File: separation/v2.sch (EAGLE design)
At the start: 0 parts

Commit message: add mcu
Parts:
- added JP2, JP4: (no value), microbuilder:HEADER-1X7
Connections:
- new net +3V3: JP4.5
- new net A0: JP2.1
- new net A1: JP2.2
- new net A2: JP2.3
- new net A3: JP2.4
- new net GND: JP4.6
- new net MISO: JP4.3
- new net MOSI: JP4.4
- new net RX: JP4.1
- new net SCK: JP4.2
- new net SCL: JP2.6
- new net SDA: JP2.5
- new net TX: JP2.7
- new net VCC: JP4.7
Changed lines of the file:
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@@
 </classes>
 <parts>
+<part name="JP2" library="microbuilder" deviceset="HEADER-1X7" device=""/>
+<part name="GND1" library="supply1" library_urn="urn:adsk.eagle:library:371" deviceset="GND" device=""/>
+<part name="JP4" library="microbuilder" deviceset="HEADER-1X7" device=""/>
+<part name="+3V1" library="supply1" library_urn="urn:adsk.eagle:library:371" deviceset="+3V3" device=""/>
 </parts>
 <sheets>
@@
 </plain>
 <instances>
+<instance part="JP2" gate="A" x="60.96" y="58.42" smashed="yes">
+<attribute name="NAME" x="54.61" y="69.215" size="1.778" layer="95"/>
+<attribute name="VALUE" x="54.61" y="45.72" size="1.778" layer="96"/>
+</instance>
+<instance part="GND1" gate="1" x="10.16" y="60.96" smashed="yes" rot="MR0">
+<attribute name="VALUE" x="12.7" y="58.42" size="1.778" layer="96" rot="MR0"/>
+</instance>
+<instance part="JP4" gate="A" x="38.1" y="58.42" smashed="yes" rot="MR180">
+<attribute name="NAME" x="31.75" y="47.625" size="1.778" layer="95" rot="MR180"/>
+<attribute name="VALUE" x="31.75" y="71.12" size="1.778" layer="96" rot="MR180"/>
+</instance>
+<instance part="+3V1" gate="G$1" x="15.24" y="60.96" smashed="yes" rot="R90">
+<attribute name="VALUE" x="20.32" y="58.42" size="1.778" layer="96" rot="R180"/>
+</instance>
 </instances>
 <busses>
 </busses>
 <nets>
+<net name="GND" class="1">
+<segment>
+<wire x1="35.56" y1="63.5" x2="10.16" y2="63.5" width="0.1524" layer="91"/>
+<pinref part="GND1" gate="1" pin="GND"/>
+<pinref part="JP4" gate="A" pin="6"/>
+</segment>
+</net>
+<net name="MOSI" class="0">
+<segment>
+<wire x1="35.56" y1="58.42" x2="17.78" y2="58.42" width="0.1524" layer="91"/>
+<label x="20.32" y="58.42" size="1.778" layer="95"/>
+<pinref part="JP4" gate="A" pin="4"/>
+</segment>
+</net>
+<net name="MISO" class="0">
+<segment>
+<wire x1="35.56" y1="55.88" x2="17.78" y2="55.88" width="0.1524" layer="91"/>
+<label x="20.32" y="55.88" size="1.778" layer="95"/>
+<pinref part="JP4" gate="A" pin="3"/>
+</segment>
+</net>
+<net name="SCK" class="0">
+<segment>
+<wire x1="35.56" y1="53.34" x2="17.78" y2="53.34" width="0.1524" layer="91"/>
+<label x="20.32" y="53.34" size="1.778" layer="95"/>
+<pinref part="JP4" gate="A" pin="2"/>
+</segment>
+</net>
+<net name="A3" class="0">
+<segment>
+<label x="45.72" y="58.42" size="1.778" layer="95"/>
+<pinref part="JP2" gate="A" pin="4"/>
+<wire x1="58.42" y1="58.42" x2="45.72" y2="58.42" width="0.1524" layer="91"/>
+</segment>
+</net>
+<net name="A2" class="0">
+<segment>
+<label x="45.72" y="60.96" size="1.778" layer="95"/>
+<pinref part="JP2" gate="A" pin="3"/>
+<wire x1="45.72" y1="60.96" x2="58.42" y2="60.96" width="0.1524" layer="91"/>
+</segment>
+</net>
+<net name="A1" class="0">
+<segment>
+<pinref part="JP2" gate="A" pin="2"/>
+<wire x1="58.42" y1="63.5" x2="45.72" y2="63.5" width="0.1524" layer="91"/>
+<label x="45.72" y="63.5" size="1.778" layer="95"/>
+</segment>
+</net>
+<net name="+3V3" class="0">
+<segment>
+<wire x1="35.56" y1="60.96" x2="17.78" y2="60.96" width="0.1524" layer="91"/>
+<pinref part="JP4" gate="A" pin="5"/>
+<pinref part="+3V1" gate="G$1" pin="+3V3"/>
+</segment>
+</net>
+<net name="A0" class="0">
+<segment>
+<label x="45.72" y="66.04" size="1.778" layer="95"/>
+<pinref part="JP2" gate="A" pin="1"/>
+<wire x1="45.72" y1="66.04" x2="58.42" y2="66.04" width="0.1524" layer="91"/>
+</segment>
+</net>
+<net name="SCL" class="0">
+<segment>
+<pinref part="JP2" gate="A" pin="6"/>
+<wire x1="58.42" y1="53.34" x2="45.72" y2="53.34" width="0.1524" layer="91"/>
+<label x="45.72" y="53.34" size="1.778" layer="95"/>
+</segment>
+</net>
+<net name="SDA" class="0">
+<segment>
+<pinref part="JP2" gate="A" pin="5"/>
+<wire x1="45.72" y1="55.88" x2="58.42" y2="55.88" width="0.1524" layer="91"/>
+<label x="45.72" y="55.88" size="1.778" layer="95"/>
+</segment>
+</net>
+<net name="TX" class="0">
+<segment>
+<pinref part="JP2" gate="A" pin="7"/>
+<wire x1="58.42" y1="50.8" x2="45.72" y2="50.8" width="0.1524" layer="91"/>
+<label x="45.72" y="50.8" size="1.778" layer="95"/>
+</segment>
+</net>
+<net name="RX" class="0">
+<segment>
+<wire x1="35.56" y1="50.8" x2="17.78" y2="50.8" width="0.1524" layer="91"/>
+<label x="20.32" y="50.8" size="1.778" layer="95"/>
+<pinref part="JP4" gate="A" pin="1"/>
+</segment>
+</net>
+<net name="VCC" class="1">
+<segment>
+<wire x1="35.56" y1="66.04" x2="17.78" y2="66.04" width="0.1524" layer="91"/>
+<wire x1="17.78" y1="66.04" x2="17.78" y2="73.66" width="0.1524" layer="91"/>
+<pinref part="JP4" gate="A" pin="7"/>
+<label x="22.86" y="73.66" size="1.778" layer="95"/>
+</segment>
+</net>
 </nets>
 </sheet>
@@
 </schematic>
 </drawing>
+<compatibility>
+<note version="8.2" severity="warning">
+Since Version 8.2, EAGLE supports online libraries. The ids
+of those online libraries will not be understood (or retained)
+with this version.
+</note>
+<note version="8.3" severity="warning">
+Since Version 8.3, EAGLE supports URNs for individual library
+assets (packages, symbols, and devices). The URNs of those assets
+will not be understood (or retained) with this version.
+</note>
+</compatibility>
 </eagle>

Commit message: 9mm buzzer
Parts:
- added LS1: KSTG931AP, SamacSys_Parts:KSTG931AP
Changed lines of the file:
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@@
 <part name="JP4" library="microbuilder" deviceset="HEADER-1X7" device=""/>
 <part name="+3V1" library="supply1" library_urn="urn:adsk.eagle:library:371" deviceset="+3V3" device=""/>
+<part name="LS1" library="SamacSys_Parts" deviceset="KSTG931AP" device="" package3d_urn="urn:adsk.eagle:package:34276129/2"/>
 </parts>
 <sheets>
@@
 <instance part="+3V1" gate="G$1" x="15.24" y="60.96" smashed="yes" rot="R90">
 <attribute name="VALUE" x="20.32" y="58.42" size="1.778" layer="96" rot="R180"/>
+</instance>
+<instance part="LS1" gate="G$1" x="119.38" y="38.1" smashed="yes">
+<attribute name="NAME" x="135.89" y="45.72" size="1.778" layer="95" align="center-left"/>
+<attribute name="VALUE" x="135.89" y="43.18" size="1.778" layer="96" align="center-left"/>
 </instance>
 </instances>
@@
 will not be understood (or retained) with this version.
 </note>
+<note version="8.3" severity="warning">
+Since Version 8.3, EAGLE supports the association of 3D packages
+with devices in libraries, schematics, and board files. Those 3D
+packages will not be understood (or retained) with this version.
+</note>
 </compatibility>

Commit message: add support components
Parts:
- added BAT: MB332-350M02SZ, SamacSys_Parts:MB332-350M02SZ
- added LDO: L7805ACV, SamacSys_Parts:L7805ACV
- renumbered LS1 to LOUD
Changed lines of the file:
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@@
 <part name="JP4" library="microbuilder" deviceset="HEADER-1X7" device=""/>
 <part name="+3V1" library="supply1" library_urn="urn:adsk.eagle:library:371" deviceset="+3V3" device=""/>
-<part name="LS1" library="SamacSys_Parts" deviceset="KSTG931AP" device="" package3d_urn="urn:adsk.eagle:package:34276129/2"/>
+<part name="LOUD" library="SamacSys_Parts" deviceset="KSTG931AP" device="" package3d_urn="urn:adsk.eagle:package:34276129/2"/>
+<part name="LDO" library="SamacSys_Parts" deviceset="L7805ACV" device="" package3d_urn="urn:adsk.eagle:package:34276127/2"/>
+<part name="BAT" library="SamacSys_Parts" deviceset="MB332-350M02SZ" device=""/>
 </parts>
 <sheets>
@@
 <attribute name="VALUE" x="20.32" y="58.42" size="1.778" layer="96" rot="R180"/>
 </instance>
-<instance part="LS1" gate="G$1" x="119.38" y="38.1" smashed="yes">
+<instance part="LOUD" gate="G$1" x="119.38" y="38.1" smashed="yes">
 <attribute name="NAME" x="135.89" y="45.72" size="1.778" layer="95" align="center-left"/>
 <attribute name="VALUE" x="135.89" y="43.18" size="1.778" layer="96" align="center-left"/>
 </instance>
+<instance part="LDO" gate="G$1" x="40.64" y="-2.54" smashed="yes">
+<attribute name="NAME" x="49.53" y="22.86" size="1.778" layer="95" align="center-left"/>
+<attribute name="VALUE" x="49.53" y="20.32" size="1.778" layer="96" align="center-left"/>
+</instance>
+<instance part="BAT" gate="G$1" x="-15.24" y="10.16" smashed="yes">
+<attribute name="NAME" x="1.27" y="17.78" size="1.778" layer="95" align="center-left"/>
+<attribute name="VALUE" x="1.27" y="15.24" size="1.778" layer="96" align="center-left"/>
+</instance>
 </instances>

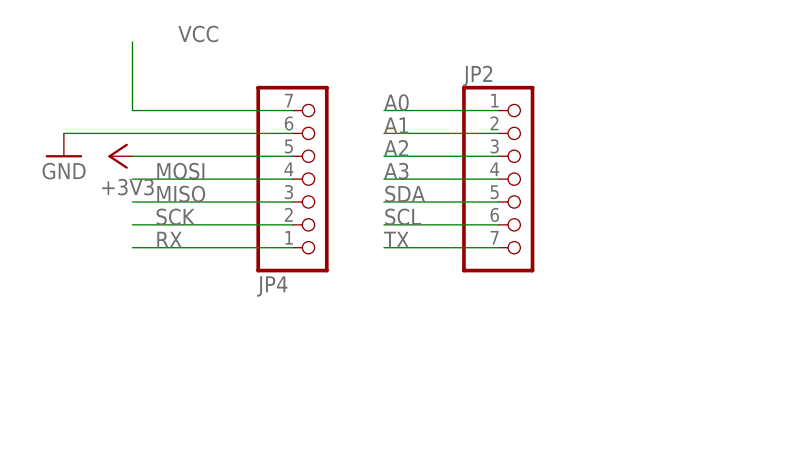
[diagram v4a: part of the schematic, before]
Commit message: rename components to be helpful
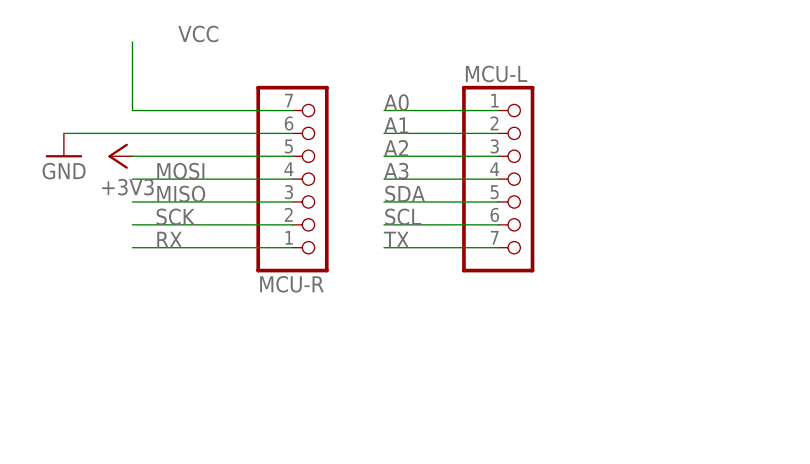
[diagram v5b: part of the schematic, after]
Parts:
- renumbered JP2 to MCU-L, JP4 to MCU-R
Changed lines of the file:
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@@
 </classes>
 <parts>
-<part name="JP2" library="microbuilder" deviceset="HEADER-1X7" device=""/>
+<part name="MCU-L" library="microbuilder" deviceset="HEADER-1X7" device=""/>
 <part name="GND1" library="supply1" library_urn="urn:adsk.eagle:library:371" deviceset="GND" device=""/>
-<part name="JP4" library="microbuilder" deviceset="HEADER-1X7" device=""/>
+<part name="MCU-R" library="microbuilder" deviceset="HEADER-1X7" device=""/>
 <part name="+3V1" library="supply1" library_urn="urn:adsk.eagle:library:371" deviceset="+3V3" device=""/>
 <part name="LOUD" library="SamacSys_Parts" deviceset="KSTG931AP" device="" package3d_urn="urn:adsk.eagle:package:34276129/2"/>
@@
 </plain>
 <instances>
-<instance part="JP2" gate="A" x="60.96" y="58.42" smashed="yes">
+<instance part="MCU-L" gate="A" x="60.96" y="58.42" smashed="yes">
 <attribute name="NAME" x="54.61" y="69.215" size="1.778" layer="95"/>
 <attribute name="VALUE" x="54.61" y="45.72" size="1.778" layer="96"/>
@@
 <attribute name="VALUE" x="12.7" y="58.42" size="1.778" layer="96" rot="MR0"/>
 </instance>
-<instance part="JP4" gate="A" x="38.1" y="58.42" smashed="yes" rot="MR180">
+<instance part="MCU-R" gate="A" x="38.1" y="58.42" smashed="yes" rot="MR180">
 <attribute name="NAME" x="31.75" y="47.625" size="1.778" layer="95" rot="MR180"/>
 <attribute name="VALUE" x="31.75" y="71.12" size="1.778" layer="96" rot="MR180"/>
@@
 <wire x1="35.56" y1="63.5" x2="10.16" y2="63.5" width="0.1524" layer="91"/>
 <pinref part="GND1" gate="1" pin="GND"/>
-<pinref part="JP4" gate="A" pin="6"/>
+<pinref part="MCU-R" gate="A" pin="6"/>
 </segment>
 </net>
@@
 <wire x1="35.56" y1="58.42" x2="17.78" y2="58.42" width="0.1524" layer="91"/>
 <label x="20.32" y="58.42" size="1.778" layer="95"/>
-<pinref part="JP4" gate="A" pin="4"/>
+<pinref part="MCU-R" gate="A" pin="4"/>
 </segment>
 </net>
@@
 <wire x1="35.56" y1="55.88" x2="17.78" y2="55.88" width="0.1524" layer="91"/>
 <label x="20.32" y="55.88" size="1.778" layer="95"/>
-<pinref part="JP4" gate="A" pin="3"/>
+<pinref part="MCU-R" gate="A" pin="3"/>
 </segment>
 </net>
@@
 <wire x1="35.56" y1="53.34" x2="17.78" y2="53.34" width="0.1524" layer="91"/>
 <label x="20.32" y="53.34" size="1.778" layer="95"/>
-<pinref part="JP4" gate="A" pin="2"/>
+<pinref part="MCU-R" gate="A" pin="2"/>
 </segment>
 </net>
@@
 <segment>
 <label x="45.72" y="58.42" size="1.778" layer="95"/>
-<pinref part="JP2" gate="A" pin="4"/>
+<pinref part="MCU-L" gate="A" pin="4"/>
 <wire x1="58.42" y1="58.42" x2="45.72" y2="58.42" width="0.1524" layer="91"/>
 </segment>
@@
 <segment>
 <label x="45.72" y="60.96" size="1.778" layer="95"/>
-<pinref part="JP2" gate="A" pin="3"/>
+<pinref part="MCU-L" gate="A" pin="3"/>
 <wire x1="45.72" y1="60.96" x2="58.42" y2="60.96" width="0.1524" layer="91"/>
 </segment>
@@
 <net name="A1" class="0">
 <segment>
-<pinref part="JP2" gate="A" pin="2"/>
+<pinref part="MCU-L" gate="A" pin="2"/>
 <wire x1="58.42" y1="63.5" x2="45.72" y2="63.5" width="0.1524" layer="91"/>
 <label x="45.72" y="63.5" size="1.778" layer="95"/>
@@
 <segment>
 <wire x1="35.56" y1="60.96" x2="17.78" y2="60.96" width="0.1524" layer="91"/>
-<pinref part="JP4" gate="A" pin="5"/>
+<pinref part="MCU-R" gate="A" pin="5"/>
 <pinref part="+3V1" gate="G$1" pin="+3V3"/>
 </segment>
@@
 <segment>
 <label x="45.72" y="66.04" size="1.778" layer="95"/>
-<pinref part="JP2" gate="A" pin="1"/>
+<pinref part="MCU-L" gate="A" pin="1"/>
 <wire x1="45.72" y1="66.04" x2="58.42" y2="66.04" width="0.1524" layer="91"/>
 </segment>
@@
 <net name="SCL" class="0">
 <segment>
-<pinref part="JP2" gate="A" pin="6"/>
+<pinref part="MCU-L" gate="A" pin="6"/>
 <wire x1="58.42" y1="53.34" x2="45.72" y2="53.34" width="0.1524" layer="91"/>
 <label x="45.72" y="53.34" size="1.778" layer="95"/>
@@
 <net name="SDA" class="0">
 <segment>
-<pinref part="JP2" gate="A" pin="5"/>
+<pinref part="MCU-L" gate="A" pin="5"/>
 <wire x1="45.72" y1="55.88" x2="58.42" y2="55.88" width="0.1524" layer="91"/>
 <label x="45.72" y="55.88" size="1.778" layer="95"/>
@@
 <net name="TX" class="0">
 <segment>
-<pinref part="JP2" gate="A" pin="7"/>
+<pinref part="MCU-L" gate="A" pin="7"/>
 <wire x1="58.42" y1="50.8" x2="45.72" y2="50.8" width="0.1524" layer="91"/>
 <label x="45.72" y="50.8" size="1.778" layer="95"/>
@@
 <wire x1="35.56" y1="50.8" x2="17.78" y2="50.8" width="0.1524" layer="91"/>
 <label x="20.32" y="50.8" size="1.778" layer="95"/>
-<pinref part="JP4" gate="A" pin="1"/>
+<pinref part="MCU-R" gate="A" pin="1"/>
 </segment>
 </net>
@@
 <wire x1="35.56" y1="66.04" x2="17.78" y2="66.04" width="0.1524" layer="91"/>
 <wire x1="17.78" y1="66.04" x2="17.78" y2="73.66" width="0.1524" layer="91"/>
-<pinref part="JP4" gate="A" pin="7"/>
+<pinref part="MCU-R" gate="A" pin="7"/>
 <label x="22.86" y="73.66" size="1.778" layer="95"/>
 </segment>

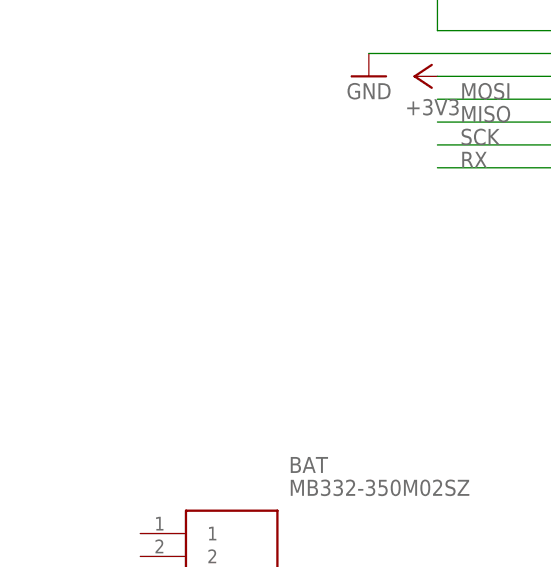
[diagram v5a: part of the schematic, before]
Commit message: servo connection
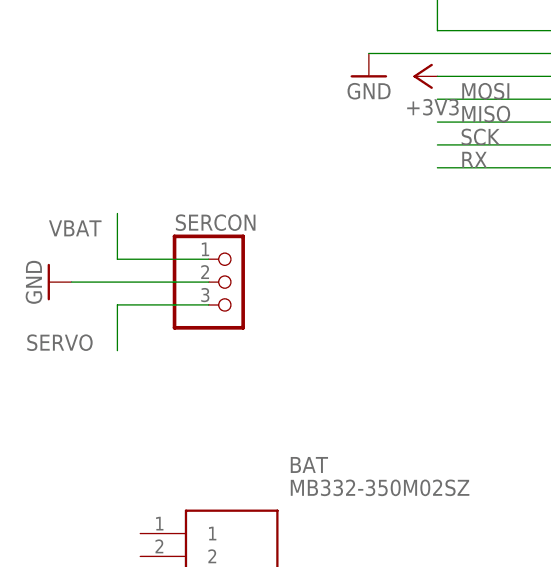
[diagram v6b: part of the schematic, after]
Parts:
- added SERCON: (no value), pinhead:PINHD-1X3
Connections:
- new net SERVO: SERCON.3
- new net VBAT: SERCON.1
- net GND: now also SERCON.2
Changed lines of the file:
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@@
 <part name="LDO" library="SamacSys_Parts" deviceset="L7805ACV" device="" package3d_urn="urn:adsk.eagle:package:34276127/2"/>
 <part name="BAT" library="SamacSys_Parts" deviceset="MB332-350M02SZ" device=""/>
+<part name="SERCON" library="pinhead" library_urn="urn:adsk.eagle:library:325" deviceset="PINHD-1X3" device="" package3d_urn="urn:adsk.eagle:package:22458/2"/>
+<part name="GND2" library="supply1" library_urn="urn:adsk.eagle:library:371" deviceset="GND" device=""/>
 </parts>
 <sheets>
@@
 <attribute name="VALUE" x="1.27" y="15.24" size="1.778" layer="96" align="center-left"/>
 </instance>
+<instance part="SERCON" gate="A" x="-5.08" y="38.1" smashed="yes">
+<attribute name="NAME" x="-11.43" y="43.815" size="1.778" layer="95"/>
+<attribute name="VALUE" x="-11.43" y="30.48" size="1.778" layer="96"/>
+</instance>
+<instance part="GND2" gate="1" x="-25.4" y="38.1" smashed="yes" rot="MR90">
+<attribute name="VALUE" x="-27.94" y="35.56" size="1.778" layer="96" rot="MR90"/>
+</instance>
 </instances>
 <busses>
@@
 <pinref part="GND1" gate="1" pin="GND"/>
 <pinref part="MCU-R" gate="A" pin="6"/>
+</segment>
+<segment>
+<pinref part="SERCON" gate="A" pin="2"/>
+<wire x1="-7.62" y1="38.1" x2="-22.86" y2="38.1" width="0.1524" layer="91"/>
+<pinref part="GND2" gate="1" pin="GND"/>
 </segment>
 </net>
@@
 </segment>
 </net>
+<net name="VBAT" class="0">
+<segment>
+<pinref part="SERCON" gate="A" pin="1"/>
+<wire x1="-7.62" y1="40.64" x2="-17.78" y2="40.64" width="0.1524" layer="91"/>
+<wire x1="-17.78" y1="40.64" x2="-17.78" y2="45.72" width="0.1524" layer="91"/>
+<label x="-25.4" y="43.18" size="1.778" layer="95"/>
+</segment>
+</net>
+<net name="SERVO" class="0">
+<segment>
+<pinref part="SERCON" gate="A" pin="3"/>
+<wire x1="-7.62" y1="35.56" x2="-17.78" y2="35.56" width="0.1524" layer="91"/>
+<wire x1="-17.78" y1="35.56" x2="-17.78" y2="30.48" width="0.1524" layer="91"/>
+<label x="-27.94" y="30.48" size="1.778" layer="95"/>
+</segment>
+</net>

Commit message: ground components
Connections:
- net GND: now also BAT.2, LDO.GND, LOUD.-
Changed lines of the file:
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@@
 <part name="SERCON" library="pinhead" library_urn="urn:adsk.eagle:library:325" deviceset="PINHD-1X3" device="" package3d_urn="urn:adsk.eagle:package:22458/2"/>
 <part name="GND2" library="supply1" library_urn="urn:adsk.eagle:library:371" deviceset="GND" device=""/>
+<part name="GND3" library="supply1" library_urn="urn:adsk.eagle:library:371" deviceset="GND" device=""/>
+<part name="GND4" library="supply1" library_urn="urn:adsk.eagle:library:371" deviceset="GND" device=""/>
+<part name="GND5" library="supply1" library_urn="urn:adsk.eagle:library:371" deviceset="GND" device=""/>
 </parts>
 <sheets>
@@
 <attribute name="VALUE" x="-27.94" y="35.56" size="1.778" layer="96" rot="MR90"/>
 </instance>
+<instance part="GND3" gate="1" x="-27.94" y="7.62" smashed="yes" rot="MR90">
+<attribute name="VALUE" x="-30.48" y="5.08" size="1.778" layer="96" rot="MR90"/>
+</instance>
+<instance part="GND4" gate="1" x="43.18" y="-12.7" smashed="yes" rot="MR0">
+<attribute name="VALUE" x="45.72" y="-15.24" size="1.778" layer="96" rot="MR0"/>
+</instance>
+<instance part="GND5" gate="1" x="106.68" y="35.56" smashed="yes" rot="MR90">
+<attribute name="VALUE" x="104.14" y="33.02" size="1.778" layer="96" rot="MR90"/>
+</instance>
 </instances>
 <busses>
@@
 <pinref part="GND2" gate="1" pin="GND"/>
 </segment>
+<segment>
+<pinref part="GND3" gate="1" pin="GND"/>
+<pinref part="BAT" gate="G$1" pin="2"/>
+<wire x1="-25.4" y1="7.62" x2="-15.24" y2="7.62" width="0.1524" layer="91"/>
+</segment>
+<segment>
+<pinref part="GND4" gate="1" pin="GND"/>
+<pinref part="LDO" gate="G$1" pin="GND"/>
+<wire x1="43.18" y1="-10.16" x2="43.18" y2="-2.54" width="0.1524" layer="91"/>
+</segment>
+<segment>
+<pinref part="GND5" gate="1" pin="GND"/>
+<pinref part="LOUD" gate="G$1" pin="-"/>
+<wire x1="109.22" y1="35.56" x2="119.38" y2="35.56" width="0.1524" layer="91"/>
+</segment>
 </net>
